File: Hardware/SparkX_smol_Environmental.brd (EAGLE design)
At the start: 10.7 x 40.6 mm, 31 parts, among them U1 SGP40, U2 BME280, U3 VEML7700-TT

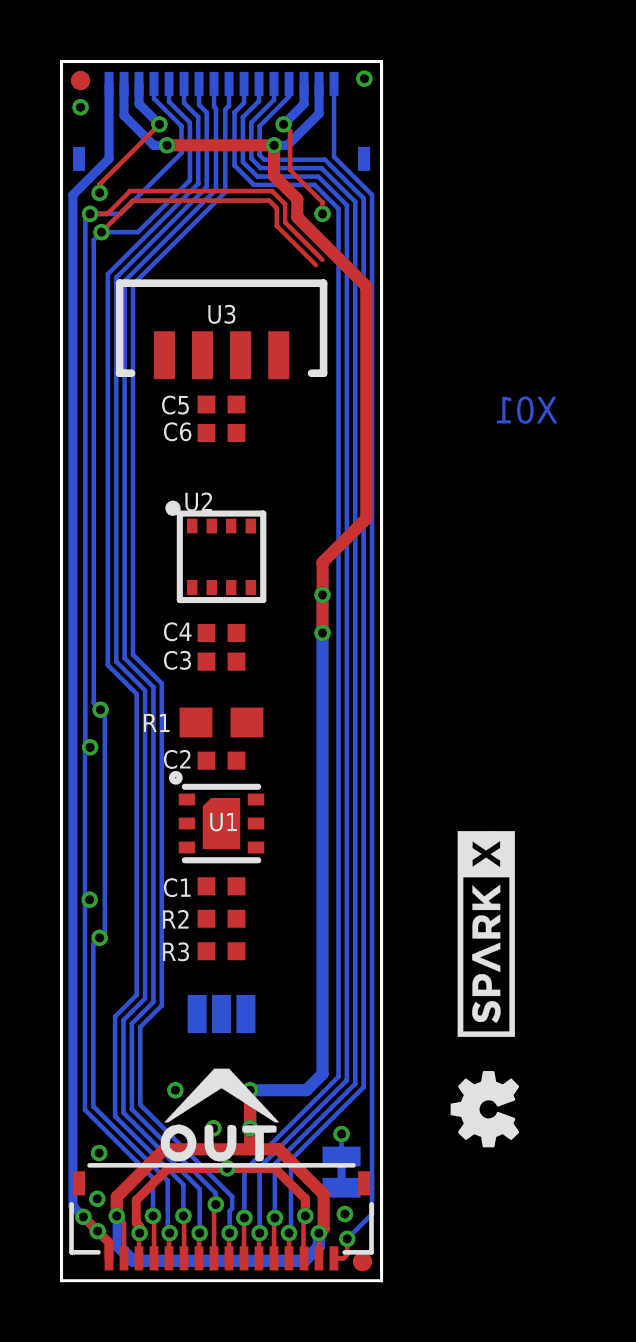
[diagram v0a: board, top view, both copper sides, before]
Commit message: Add production files and README
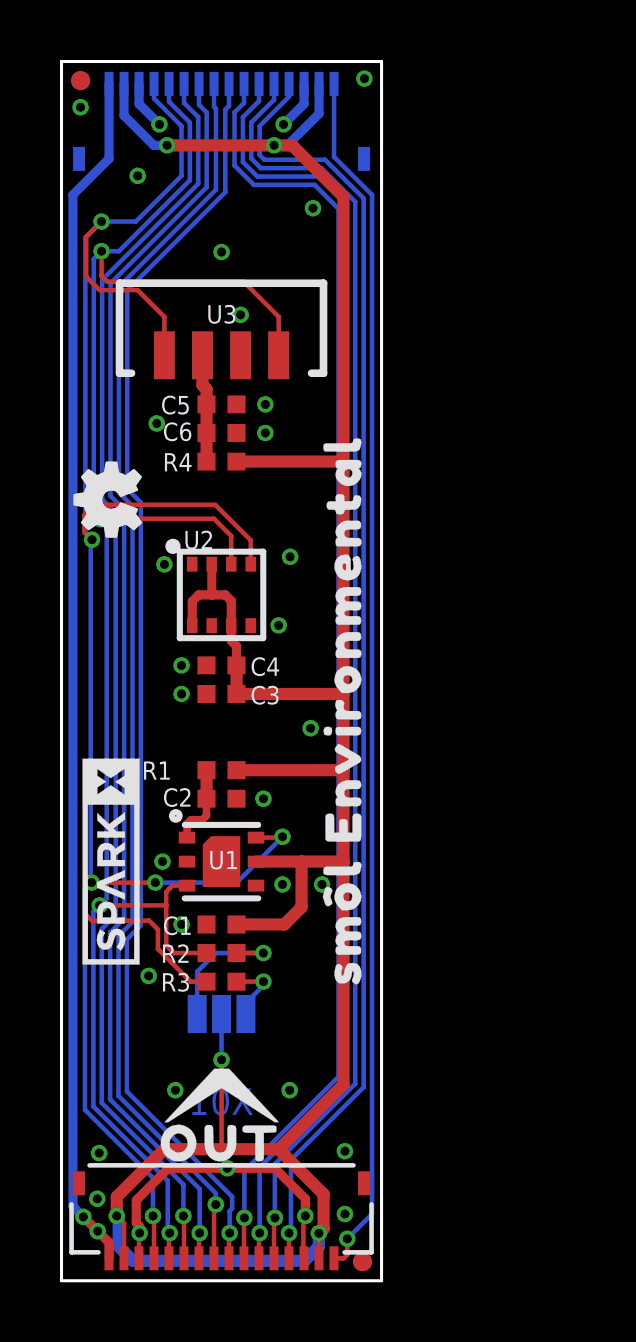
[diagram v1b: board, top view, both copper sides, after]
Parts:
- removed PROC_PWR_EN: JUMPER-SMT_2_NC_TRACE_SILK, SparkFun-Jumpers:SMT-JUMPER_2_NC_TRACE_SILK
- removed U$7: (no value), output:#PROC_PWR#0
- added R4: 4.7, SparkFun-Resistors:0402-TIGHT
- added U$2, U$4: (no value), output:SM�L_ENVIRONMENTAL0
- added U$5: (no value), output:#I�C#0
- R1: device SparkFun-Resistors:0603 -> SparkFun-Resistors:0402-TIGHT
- moved LOGO2 23.9 mm to (1.65, 26.0)
- moved U$1 12.7 mm to (1.65, 14.0)
- moved U$20 3.81 mm to (5.33, 21.6), turned to 90 degrees
- moved LOGO3 2.87 mm to (8.13, 21.6), turned to 90 degrees
- moved R1 1.59 mm to (5.33, 17.0)
- moved C1 1.27 mm to (5.33, 11.9)
- moved C2 1.27 mm to (5.33, 16.1)
- moved U1 1.27 mm to (5.33, 14.0)
- moved U2 1.27 mm to (5.33, 22.9)
- moved R2 1.14 mm to (5.33, 10.9)
- moved C3 1.08 mm to (5.33, 19.6), turned to 180 degrees
- moved C4 1.08 mm to (5.33, 20.5), turned to 180 degrees
- moved R3 1.02 mm to (5.33, 9.97)
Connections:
- new net N$4: C5.1, C6.1, R4.1, U3.2
- net 3.3V: now also R4.2; no longer C5.1, C6.1, U3.2
- net GND: no longer PROC_PWR_EN.2
- net PROC_PWR_EN: no longer PROC_PWR_EN.1
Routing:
- net 3.3V: track 70.5 -> 94.7 mm, vias 8 -> 5
- net SCL: track 52.0 -> 71.5 mm, vias 4 -> 6
- net SDA: track 51.7 -> 62.9 mm
- net GND: track 21.2 -> 13.8 mm, vias 15 -> 32
- net N$2: track 0.00 -> 4.77 mm, vias 0 -> 1
- net N$4: track 0.00 -> 3.60 mm
- net N$1: track 0.00 -> 2.74 mm
- net N$3: track 0.00 -> 2.22 mm, vias 0 -> 1
- net PROC_PWR_EN: track 41.4 -> 40.4 mm
